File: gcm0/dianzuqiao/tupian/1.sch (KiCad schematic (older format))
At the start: 69 parts, among them Q1 BC547, Q2 BC547, Q3 BC547, Q4 BC547, U1 LM317_TO3, U2 LM7805_TO220, U3 LM1117-3.3, U4 LM2576S-ADJ, U5 STM32F030F4P6, U6 74HC595, U7 74HC595, U8 NE5532, U9 TL084, Y1 8M

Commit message: 电路改错1
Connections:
- net +3.3: now also U5.16 (VDD), U5.5 (VDDA)
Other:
- moved on the sheet: U9C
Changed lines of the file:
@@
 EESchema Schematic File Version 4
+LIBS:1-cache
 EELAYER 29 0
 EELAYER END
@@
 L Amplifier_Operational:TL084 U9
 U 3 1 5DBA31C2
-P 11350 7050
-F 0 "U9" H 11350 7417 50  0000 C CNN
-F 1 "TL084" H 11350 7326 50  0000 C CNN
-F 2 "" H 11300 7150 50  0001 C CNN
-F 3 "http://www.ti.com/lit/ds/symlink/tl081.pdf" H 11400 7250 50  0001 C CNN
-	3    11350 7050
+P 11300 7050
+F 0 "U9" H 11300 7417 50  0000 C CNN
+F 1 "TL084" H 11300 7326 50  0000 C CNN
+F 2 "" H 11250 7150 50  0001 C CNN
+F 3 "http://www.ti.com/lit/ds/symlink/tl081.pdf" H 11350 7250 50  0001 C CNN
+	3    11300 7050
 	-1   0    0    1
 $EndComp
@@
 	12200 6250 12350 6250
 Connection ~ 12350 6250
-Wire Wire Line
-	11650 6950 11800 6950
 $Comp
 L power:GND #PWR?
@@
 Wire Wire Line
 	11800 6950 11800 6250
+Wire Wire Line
+	11600 6950 11800 6950
 Connection ~ 11800 6250
 Wire Wire Line
@@
 	11800 7150 11800 8200
 Wire Wire Line
-	11650 7150 11800 7150
+	11600 7150 11800 7150
 Connection ~ 11800 8200
 Wire Wire Line
 	11800 8200 11900 8200
 Wire Wire Line
-	11050 7050 11000 7050
+	11000 7050 10900 7050
 Wire Wire Line
 	11000 6250 11000 7050
@@
 Connection ~ 11000 7050
 Wire Wire Line
-	11000 7050 10900 7050
+	6200 5300 6200 5150
+Wire Wire Line
+	6200 5150 6100 5150
+Wire Wire Line
+	6100 5150 6100 5300
+Wire Wire Line
+	6200 5150 6300 5150
+Connection ~ 6200 5150
+Text GLabel 6300 5150 2    50   Input ~ 0
++3.3
 $EndSCHEMATC

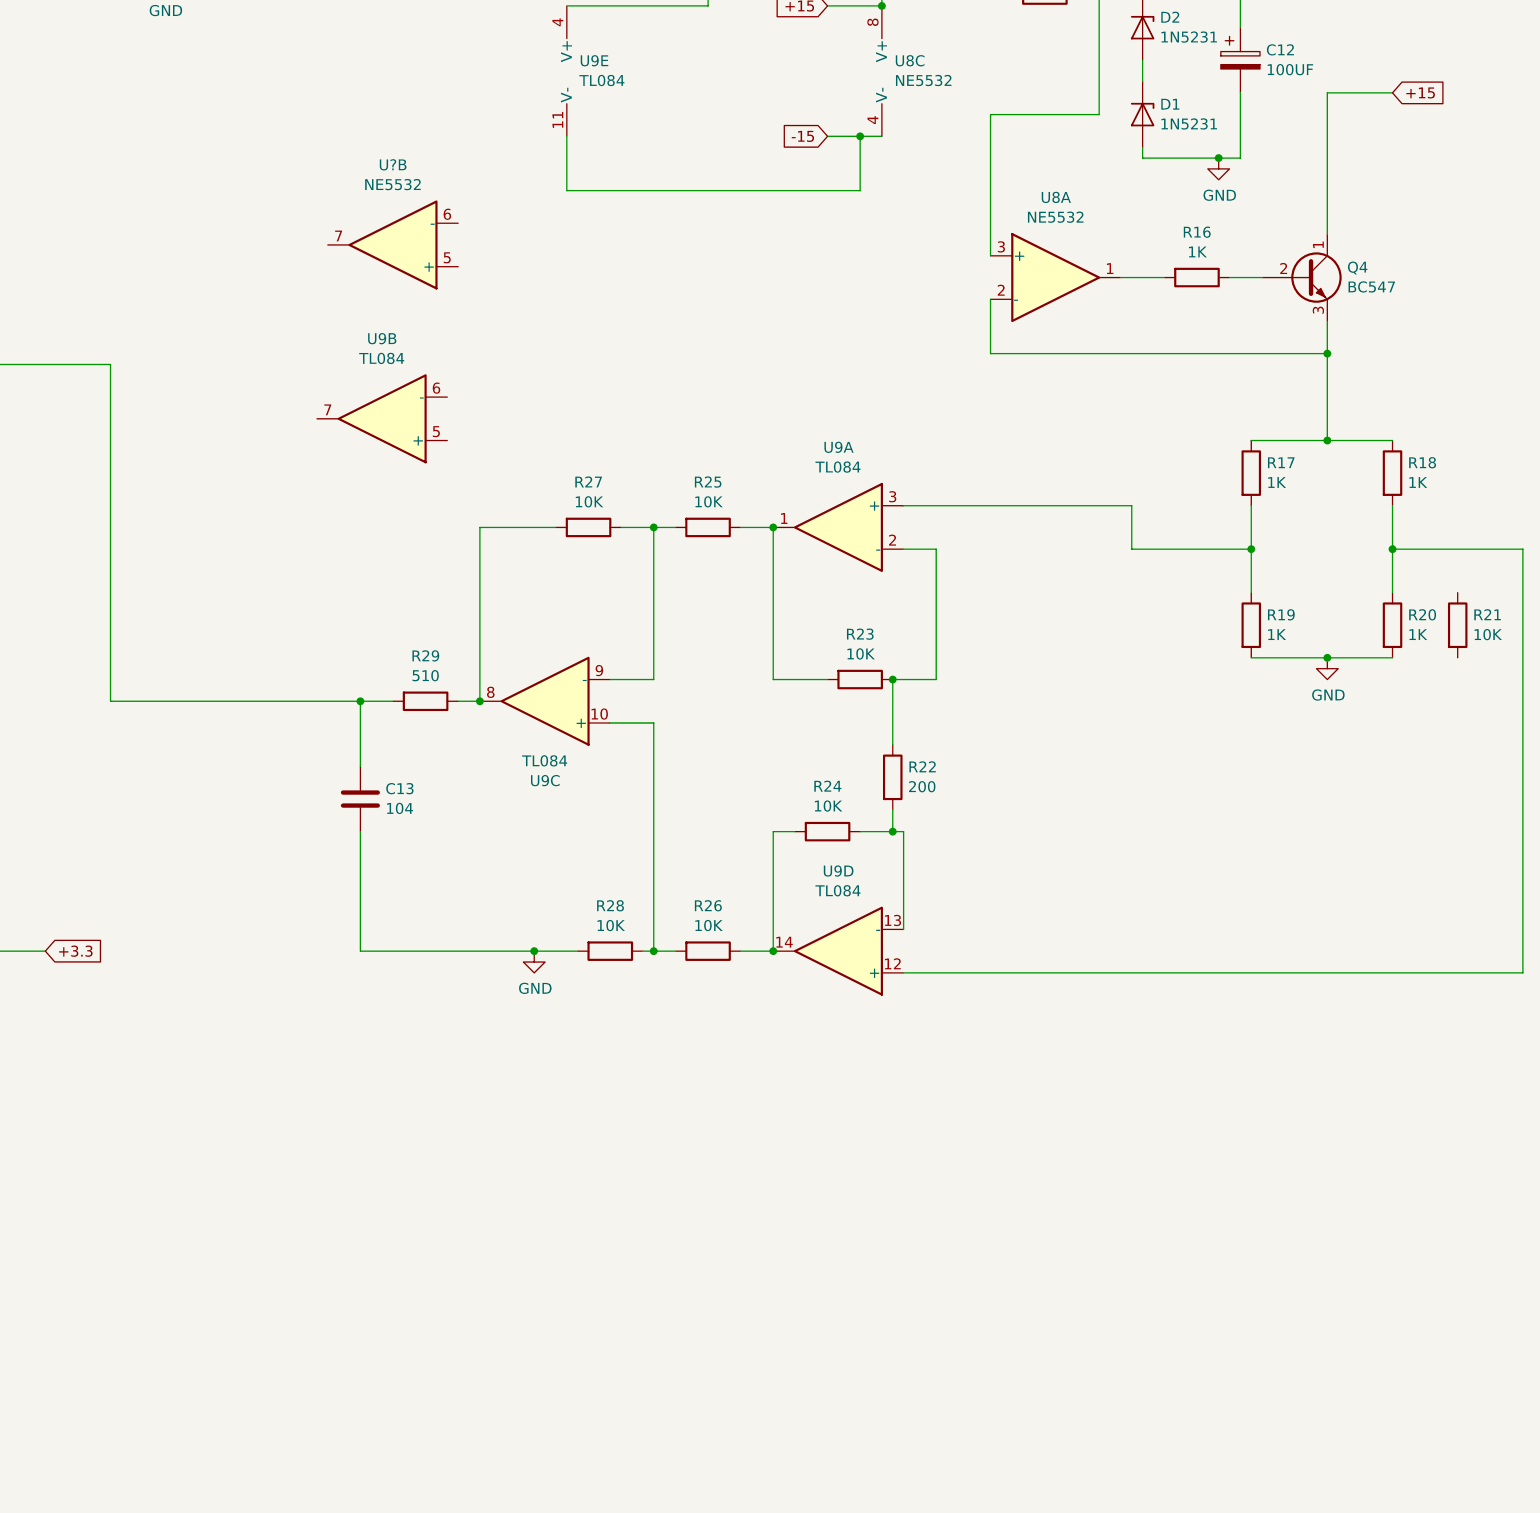
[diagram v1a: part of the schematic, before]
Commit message: 接上称重传感器
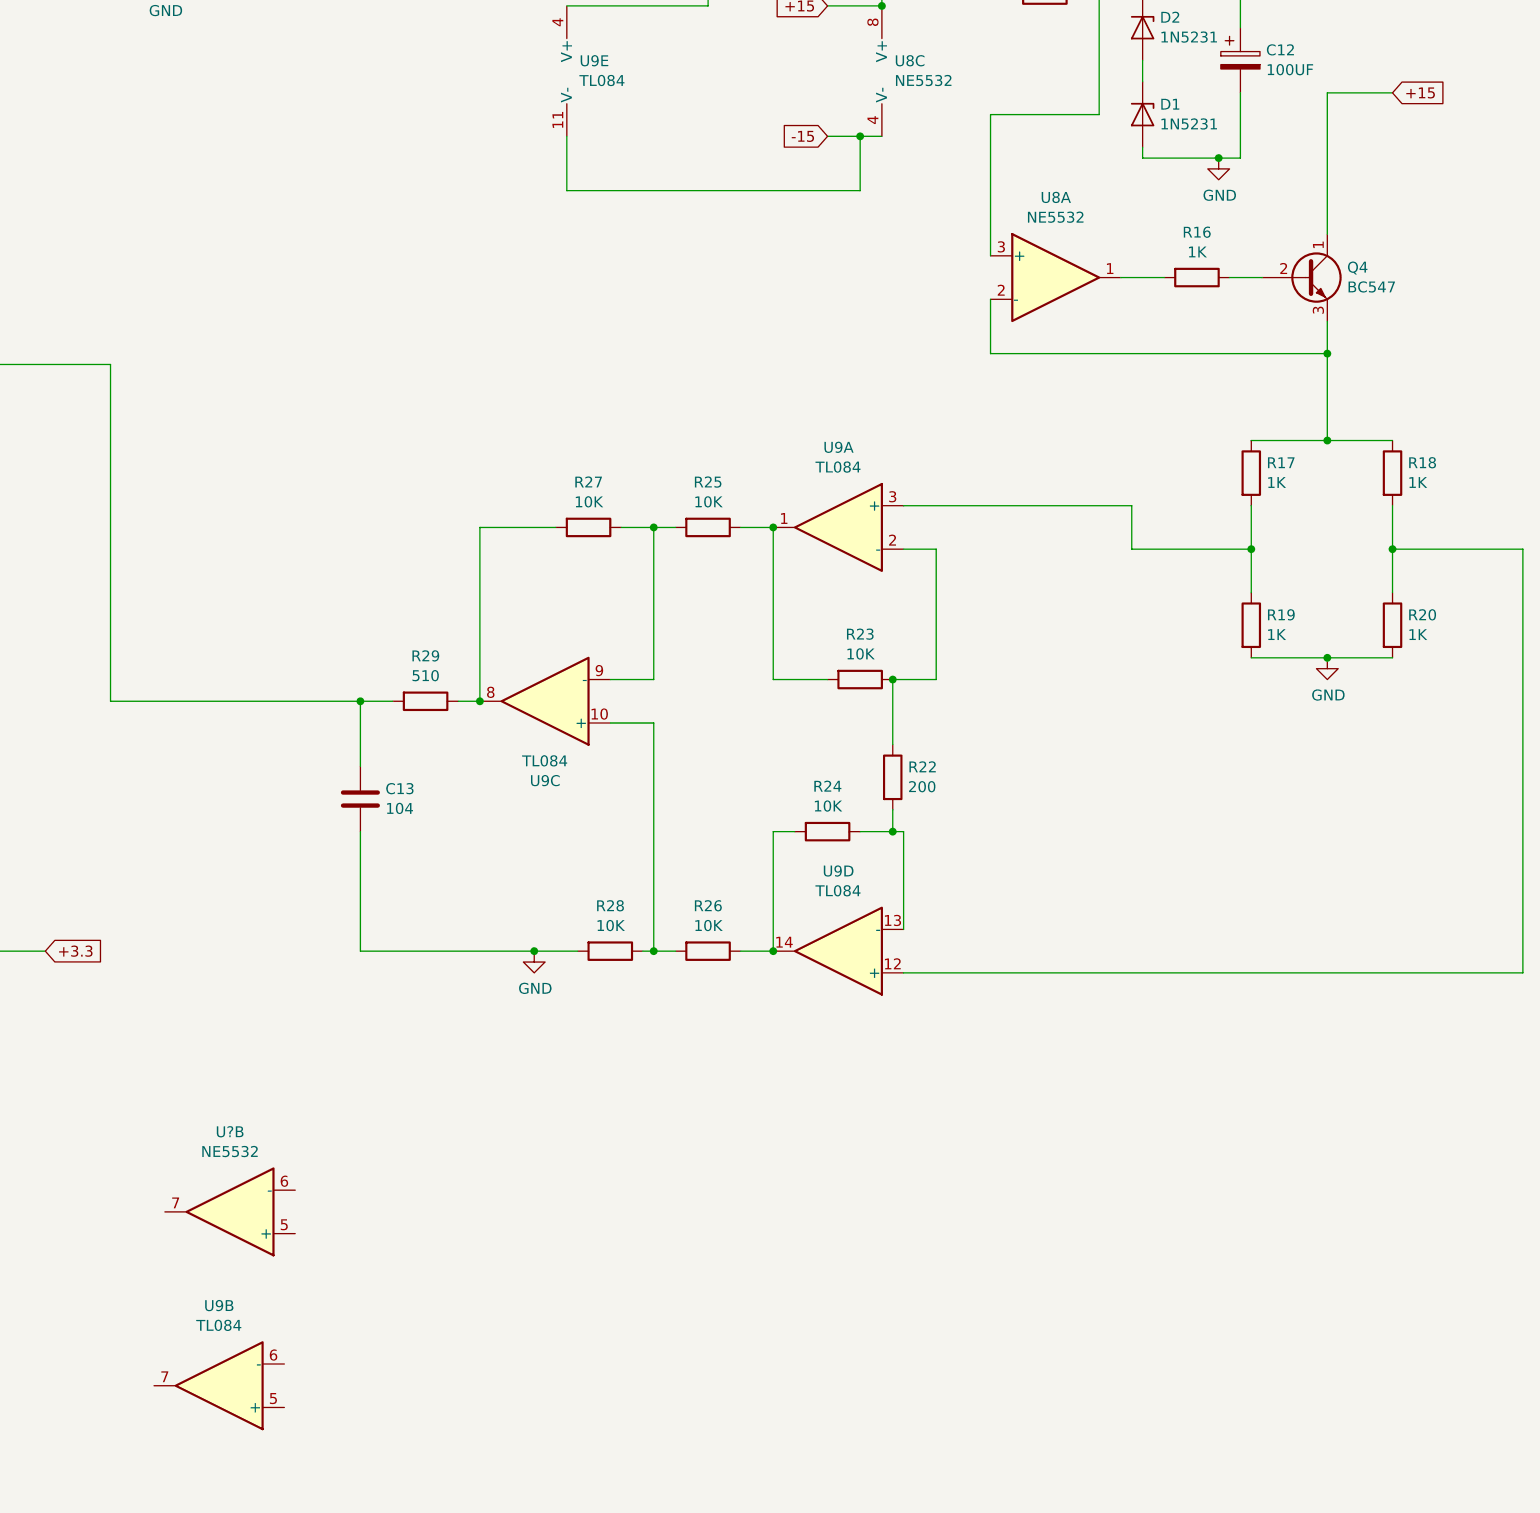
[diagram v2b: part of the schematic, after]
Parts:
- removed R21: 10K, symbol Device:R
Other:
- moved on the sheet: U9B, U?B
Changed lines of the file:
@@
 L Amplifier_Operational:TL084 U9
 U 2 1 5DB9F053
-P 10550 5750
-F 0 "U9" H 10550 5383 50  0000 C CNN
-F 1 "TL084" H 10550 5474 50  0000 C CNN
-F 2 "" H 10500 5850 50  0001 C CNN
-F 3 "http://www.ti.com/lit/ds/symlink/tl081.pdf" H 10600 5950 50  0001 C CNN
-	2    10550 5750
+P 9800 10200
+F 0 "U9" H 9800 9833 50  0000 C CNN
+F 1 "TL084" H 9800 9924 50  0000 C CNN
+F 2 "" H 9750 10300 50  0001 C CNN
+F 3 "http://www.ti.com/lit/ds/symlink/tl081.pdf" H 9850 10400 50  0001 C CNN
+	2    9800 10200
 	-1   0    0    1
 $EndComp
@@
 	9300 7050 10450 7050
 Connection ~ 10450 7050
-$Comp
-L Device:R R21
-U 1 1 5E19E259
-P 15500 6700
-F 0 "R21" H 15570 6746 50  0000 L CNN
-F 1 "10K" H 15570 6655 50  0000 L CNN
-F 2 "" V 15430 6700 50  0001 C CNN
-F 3 "~" H 15500 6700 50  0001 C CNN
-	1    15500 6700
-	1    0    0    -1
-$EndComp
 Wire Wire Line
 	15800 6350 15800 8300
 Wire Wire Line
 	12950 8300 15800 8300
-Wire Wire Line
-	15200 6350 15800 6350
 $Comp
 L Amplifier_Operational:NE5532 U?
 U 2 1 5E22D8E4
-P 10600 4950
-F 0 "U?" H 10600 4583 50  0000 C CNN
-F 1 "NE5532" H 10600 4674 50  0000 C CNN
-F 2 "" H 10600 4950 50  0001 C CNN
-F 3 "http://www.ti.com/lit/ds/symlink/ne5532.pdf" H 10600 4950 50  0001 C CNN
-	2    10600 4950
+P 9850 9400
+F 0 "U?" H 9850 9033 50  0000 C CNN
+F 1 "NE5532" H 9850 9124 50  0000 C CNN
+F 2 "" H 9850 9400 50  0001 C CNN
+F 3 "http://www.ti.com/lit/ds/symlink/ne5532.pdf" H 9850 9400 50  0001 C CNN
+	2    9850 9400
 	-1   0    0    1
 $EndComp
@@
 Text GLabel 6300 5150 2    50   Input ~ 0
 +3.3
+Wire Wire Line
+	15200 6350 15800 6350
 $EndSCHEMATC
